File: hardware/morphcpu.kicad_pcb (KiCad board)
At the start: 2 copper layers, 70 x 70 mm, 84 parts, among them J1 TYPE-C-31-M-12, SW1 TS-1187A-B-A-B, U1 ICE40UP5K-SG48I, U2 FT231XS-R, U3 W25Q32JVSSIQ, U4 ME6211C33M5G-N, U5 ME6211C12M5G-N, U6 USBLC6-2SC6, X1 1532H4-16000JWPDTSNL

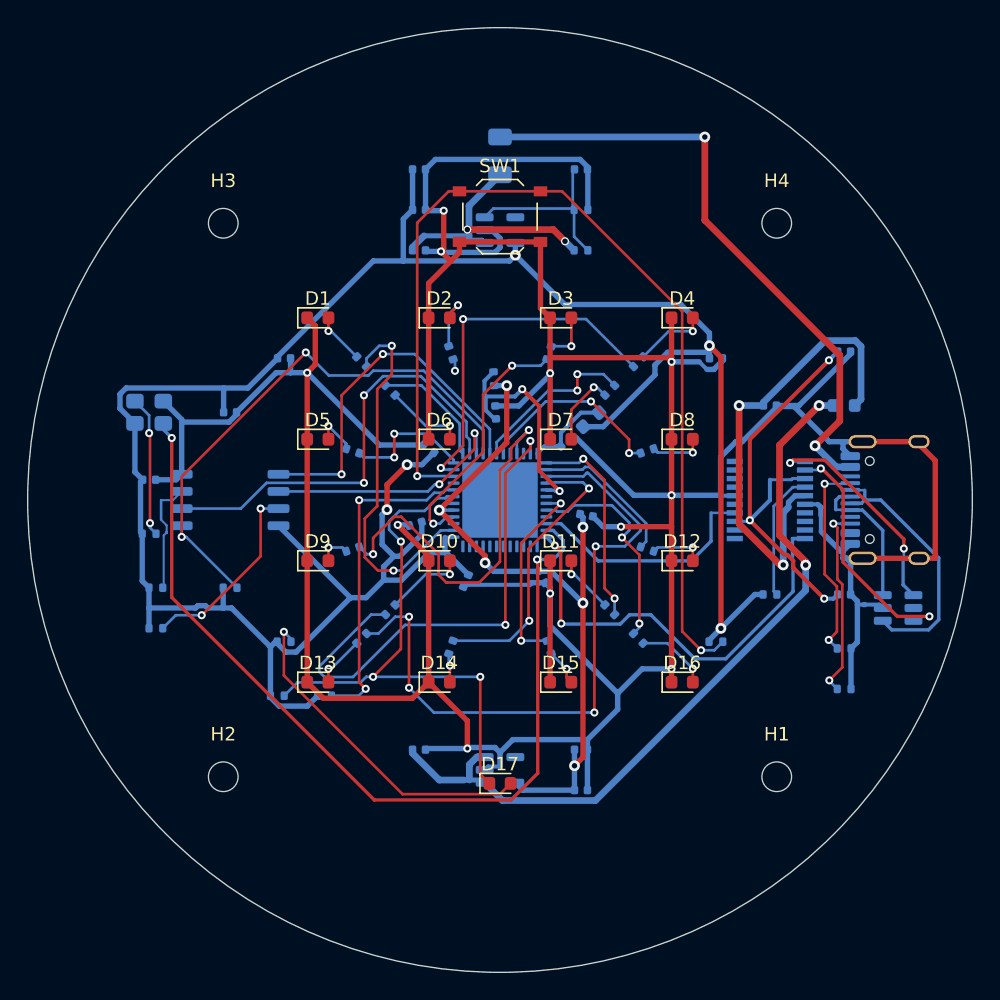
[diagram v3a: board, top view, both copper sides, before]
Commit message: autoroute revert
board back to 0 tracks 0 zones. freerouting didnt come back clean and the front
face was a mess, so its out. kept the DSN, the SES and the renders, wrote up
what happened in ROUTING.md.

DRC after: 1 cosmetic silk, 167 unconnected. ERC 0/0. generators run, tests pass.

also went over every .md .py .sh .v .pcf .scad. contractions, unicode arrows to
ascii, comment divider scaffolding out. no number or part number or path
changed, tables left alone, $display and RESULT:/PASS: strings untouched cause
run_sims.sh reads them.
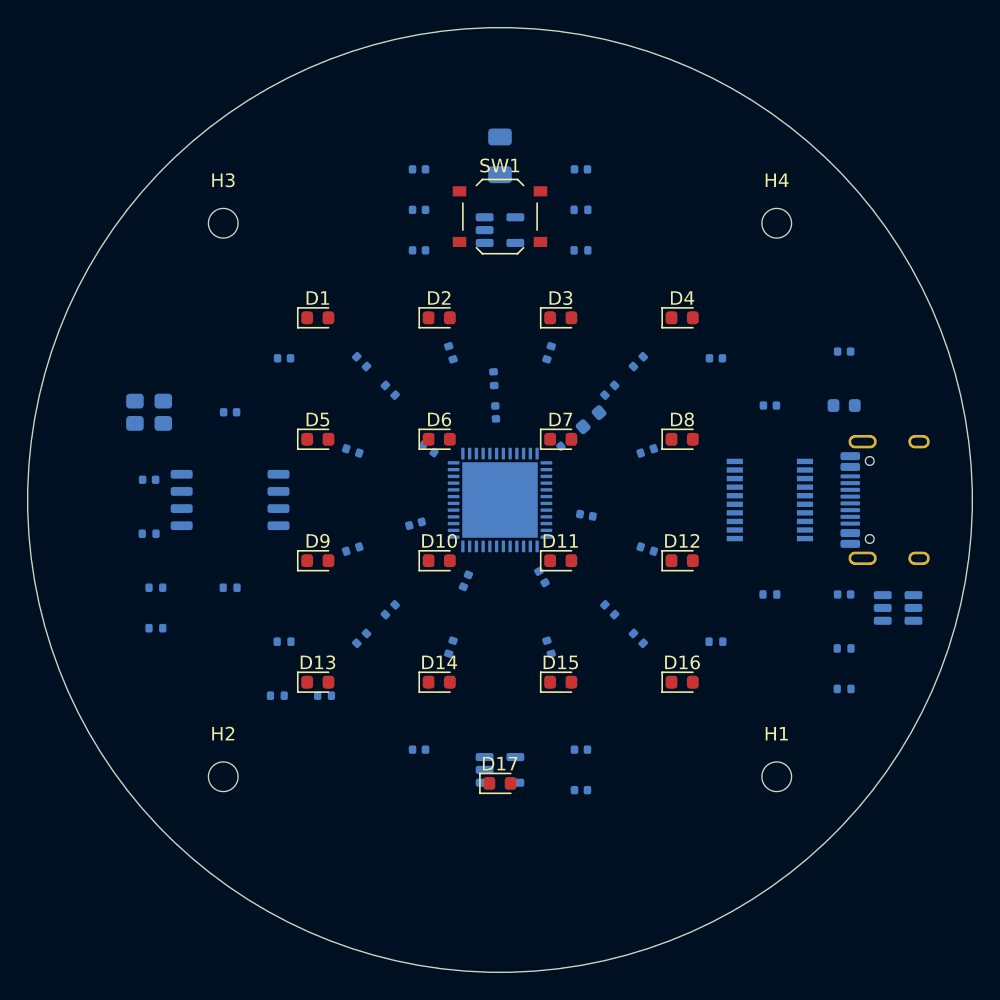
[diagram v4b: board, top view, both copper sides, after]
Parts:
- turned C2 to -61.4286 degrees
- turned C4 to -164.286 degrees
- turned C21 to 41.4286 degrees
- turned R8 to 18.4349 degrees
- turned R14 to -108.435 degrees
- turned R12 to -18.4349 degrees
- turned R15 to -71.5651 degrees
- turned R2 to 108.435 degrees
- turned R5 to 161.565 degrees
- turned R3 to 71.5651 degrees
- turned R9 to -161.565 degrees
- turned C5 to 144.286 degrees
- turned C3 to -112.857 degrees
- turned C20 to 92.8571 degrees
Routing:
- net GND: track 339.1 -> 0.00 mm, vias 11 -> 0
- net +3V3: track 183.2 -> 0.00 mm, vias 5 -> 0
- net VBUS: track 77.1 -> 0.00 mm, vias 4 -> 0
- net RST_N: track 73.3 -> 0.00 mm, vias 2 -> 0
- net CLK: track 67.6 -> 0.00 mm, vias 2 -> 0
- net +1V2: track 53.7 -> 0.00 mm, vias 6 -> 0
- net LED12: track 48.7 -> 0.00 mm, vias 4 -> 0
- net VBUS_IN: track 46.2 -> 0.00 mm, vias 2 -> 0
- net CDONE: track 41.6 -> 0.00 mm, vias 3 -> 0
- net FLASH_CS: track 41.5 -> 0.00 mm, vias 2 -> 0
- net LED9: track 37.8 -> 0.00 mm, vias 2 -> 0
- net FT_VCC: track 35.5 -> 0.00 mm, vias 2 -> 0
- net UART_RX_I: track 33.5 -> 0.00 mm, vias 2 -> 0
- net FLASH_DO: track 32.8 -> 0.00 mm, vias 2 -> 0
- net FT_3V3: track 32.0 -> 0.00 mm, vias 3 -> 0
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
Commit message: 4 layers / board routes now
2 layers was the problem, not the router. the resistor ring sits at r 11-15 and
the decap ring at r 6-7, both inside the F.Cu keepout, so all 16 LED escapes
plus every supply converging on U1 had exactly one layer to share. seven
freerouting configs, a maze router, a rip-up loop and a pathfinder
implementation all bounced off that.

stackup is F.Cu / In1.Cu / In2.Cu / B.Cu, both inner layers signal. In1 was a
power plane first and freerouting wont route on a power layer, so it only used
In2 and came back at 13 unrouted. flipping In1 to signal got it to 11

  DRC   1 violation, the same cosmetic C20/R27 silk overlap thats been there
        since the resistor ring moved. zero clearance, zero hole, zero thermal
  unconnected  17 items

  F.Cu    39 segments
  In1.Cu  77
  In2.Cu 100
  B.Cu   366
  vias   130

front face is clean and it actually verifies now:

  keepout violations in DRC                            0
  F.Cu segments with copper in the no-track region     0

checked twice, once by DRC and once by walking 20 points along every F.Cu
segment against the escape windows. 39 F.Cu segments on the whole board and
none of them cross the display

min track width went 0.1524 -> 0.127. freerouting kept emitting 0.15 mm and 5
mil is JLC's economical tier for 2 layer anyway, so its free. that cleared 10
track_width errors

the 17 unconnected are 5 connections my router couldnt place, all U1 escapes,
U1-30 to C1-1, U1-30 to U1-5, U1-29 to C20-1, R13-1 to U1-27, R16-1 to U1-32,
plus a VBUS_IN via that needs a pad. hand route them, theyre short

LED2 got routed and then ripped back out, 139 segments of meander that pulled
12 clearance errors with it. one connection for twelve violations wasnt worth
keeping

what didnt work, so nobody repeats it. narrower traces made it worse, 15 -> 18.
300 passes and a different search strategy gave byte identical output to 100
passes. a centre disc in the keepout bought exactly one net. grafting a route
back 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
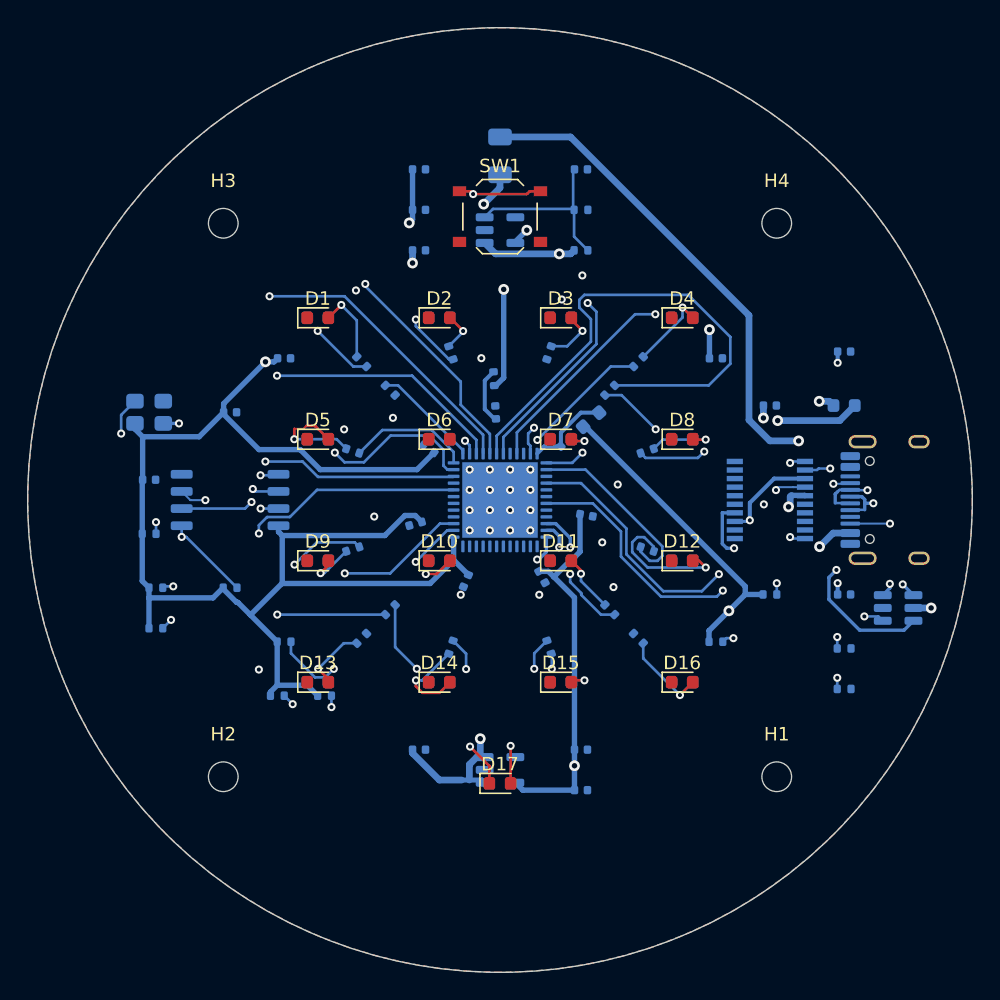
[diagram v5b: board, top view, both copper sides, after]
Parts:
- turned C2 to -61.429 degrees
- turned C4 to -164.286 degrees
- turned C21 to 41.429 degrees
- turned R8 to 18.435 degrees
- turned R14 to -108.435 degrees
- turned R12 to -18.435 degrees
- turned R15 to -71.565 degrees
- turned R2 to 108.435 degrees
- turned R5 to 161.565 degrees
- turned R3 to 71.565 degrees
- turned R9 to -161.565 degrees
- turned C5 to 144.286 degrees
- turned C3 to -112.857 degrees
- turned C20 to 92.857 degrees
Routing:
- net +3V3: track 0.00 -> 194.9 mm, vias 0 -> 5
- net VBUS: track 0.00 -> 119.3 mm, vias 0 -> 6
- net RST_N: track 0.00 -> 92.5 mm, vias 0 -> 3
- net +1V2: track 0.00 -> 72.8 mm, vias 0 -> 2
- net LED8: track 0.00 -> 68.1 mm, vias 0 -> 5
- net FLASH_CS: track 0.00 -> 49.2 mm, vias 0 -> 2
- net VBUS_IN: track 0.00 -> 47.2 mm, vias 0 -> 2
- net LED0: track 0.00 -> 47.0 mm, vias 0 -> 2
- net LED13: track 0.00 -> 41.9 mm, vias 0 -> 2
- net LED9: track 0.00 -> 40.1 mm, vias 0 -> 3
- net LED6: track 0.00 -> 38.5 mm
- net FLASH_DI: track 0.00 -> 36.5 mm, vias 0 -> 2
- net LED3: track 0.00 -> 36.4 mm, vias 0 -> 2
- net LED14: track 0.00 -> 36.1 mm, vias 0 -> 2
- net CLK: track 0.00 -> 35.9 mm, vias 0 -> 2
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- added copper zone on B.Cu, net GND
- added copper zone on F.Cu, net GND
- added copper zone on In1.Cu, net GND
- added copper zone on In2.Cu, net GND
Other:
- copper layers 2 -> 4

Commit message: route 7 of the 17 outstanding connections, DRC to 0 violations
Adds 84 segments and 11 vias for seven connections: the GND pour fragments at
C4.2, C12.2 and C7.2 (C7 also resolves U3.4, same island), plus VCCPLL_F,
VBUS_IN, LED2 and LED15. Nothing already on the board was moved.

Every placed segment and via was exact-clearance checked against all foreign
copper before being committed, and the no-track rule area is honoured as
outline-minus-holes. VBUS_IN came out at 0.30 mm against its 0.50 mm PWR_5V
class - still 1.00 A by IPC-2221 against a 500 mA polyfuse, but it drops the
intended ~2.9x margin to ~2x, so it is worth a look by hand.

Also moves C20's reference field 1.3 mm in X, clearing the silk overlap with
R27 that was the last standing violation.

DRC, with the .kicad_pro alongside: 1 violation / 17 unconnected -> 0 / 10.

Six of the ten that remain cannot be routed by adding copper at all - U1.22
has 51 reachable grid cells and no via fits - and need the U1 fanout ripped up
first. ROUTING.md records the per-connection reachability analysis and why
both a grid maze router and a second Freerouting pass fell short.
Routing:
- net LED2: track 0.00 -> 22.3 mm, vias 0 -> 3
- net LED15: track 0.00 -> 12.2 mm, vias 0 -> 2
- net VCCPLL_F: track 4.16 -> 14.8 mm, vias 0 -> 2
- net VBUS_IN: track 47.2 -> 53.1 mm, vias 2 -> 3
- net GND: track 0.00 -> 2.41 mm, vias 24 -> 27

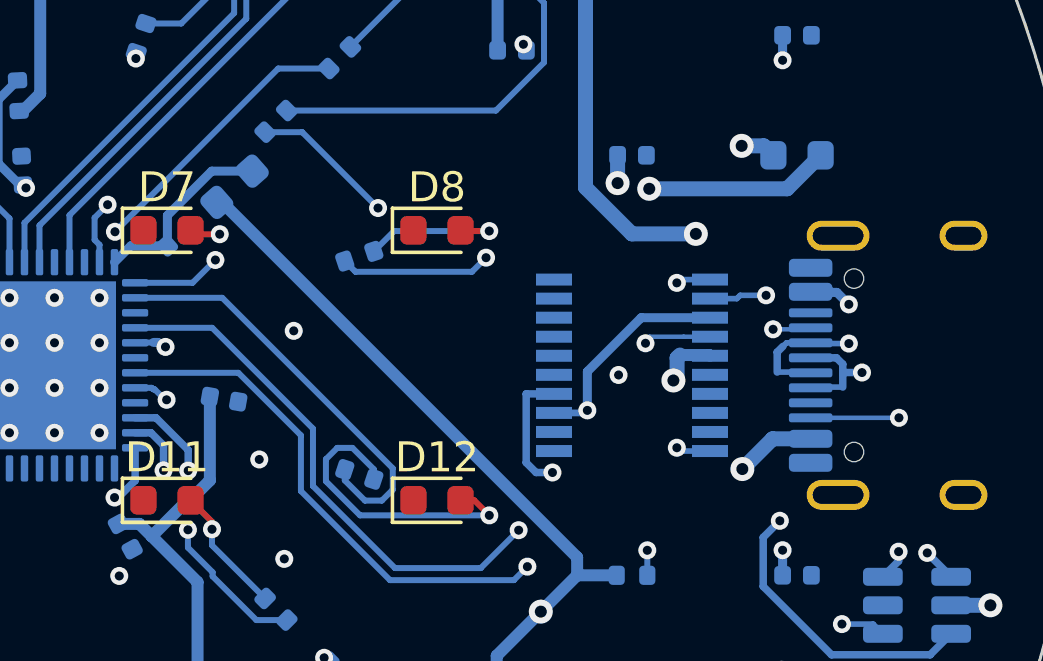
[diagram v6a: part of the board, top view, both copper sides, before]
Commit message: route 2 of the 10 outstanding: GND at C21.2 and U2.16
Both pads sit in a small isolated B.Cu pour island with the main In1/In2/F
planes running straight underneath, so what they needed was one stitching via
each, not a route. Neither had a legal through-via site: a via must clear all
four layers, and the inner layers were covered.

C21.2 had four free sites all along - the earlier search missed them because
the 0.05 mm raster marks a cell blocked when its centre falls inside the
inflated obstacle, which is up to half a cell pessimistic. The router now
rasterises half a cell optimistic and lets exact pcbnew clearance be the
authority, vetoing rejected cells and re-routing.

U2.16 was walled on In2 by the VBUS_IN leg running down the middle of its
pocket, so VBUS_IN was ripped and rebuilt around the new via. That also lifts
VBUS_IN off the 0.30 mm it had necked to; it is 0.40 mm now against its
0.50 mm PWR_5V class.

USB_DP/DM and CC1/CC2 verified byte-identical.

0 violations, 10 unconnected -> 0 violations, 8 unconnected.
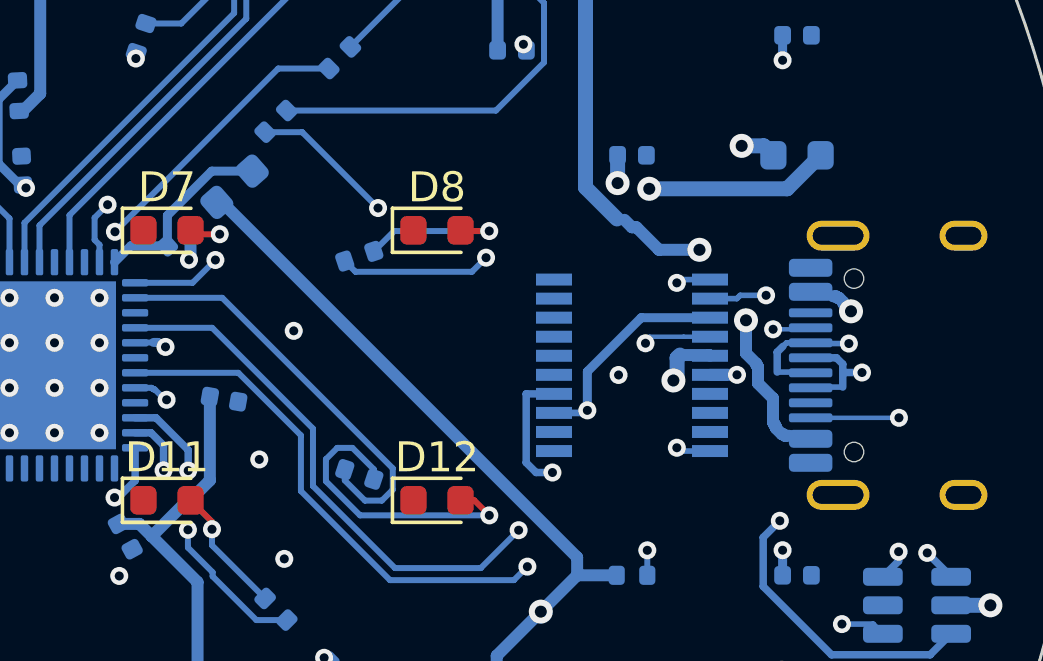
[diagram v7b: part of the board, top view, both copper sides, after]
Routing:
- net VBUS_IN: track 53.1 -> 49.6 mm
- net GND: track 2.41 -> 4.70 mm, vias 27 -> 29

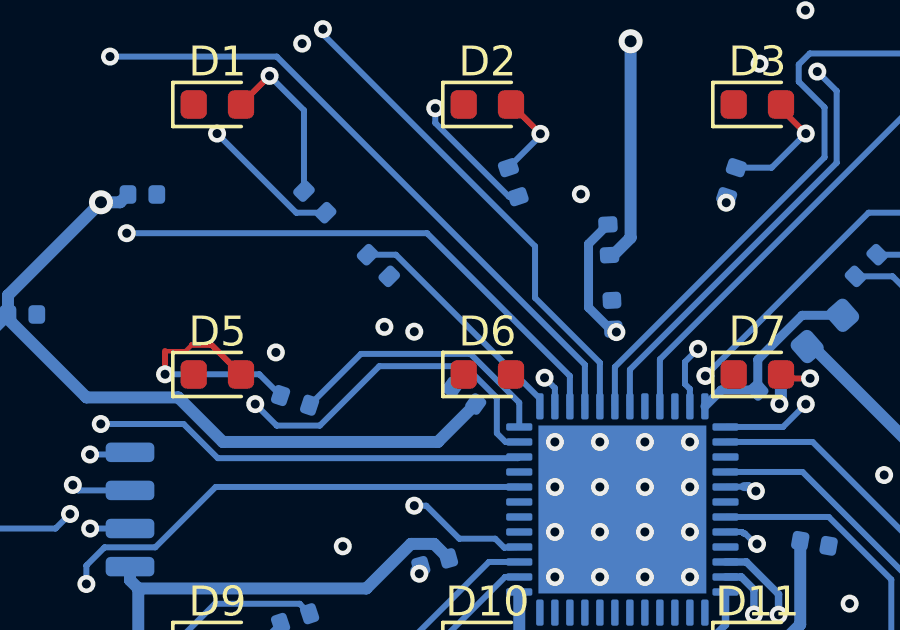
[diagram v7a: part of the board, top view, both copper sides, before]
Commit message: route LED5_A, the last one that did not need the U1 fanout moved
Falls out standalone now that the router rasterises half a cell optimistic and
lets exact pcbnew clearance arbitrate. 8 segments and 3 vias, R6.2 on B.Cu up
to D6.2 on F.Cu.

0 violations, 8 unconnected -> 0 violations, 7 unconnected.
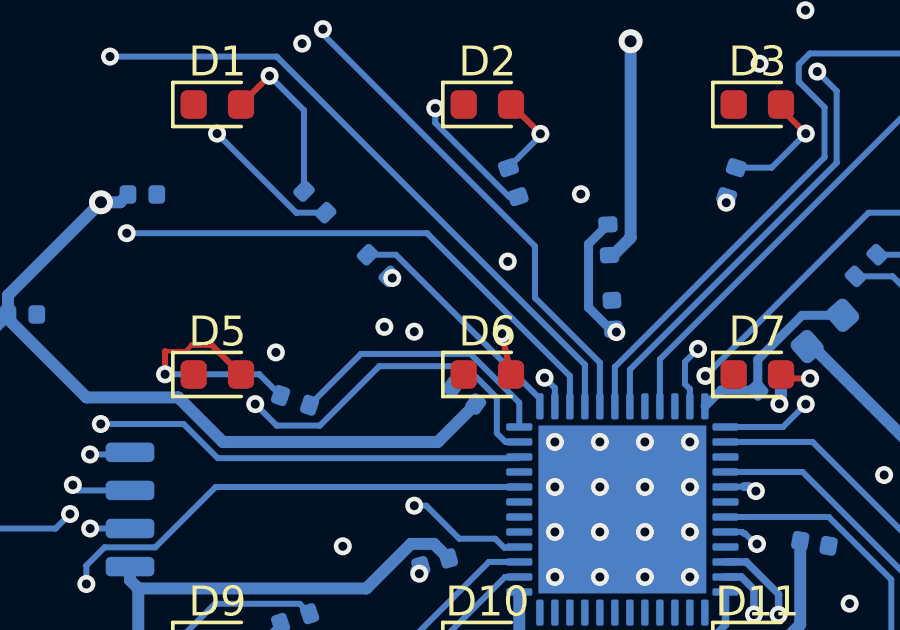
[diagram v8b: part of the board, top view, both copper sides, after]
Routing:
- net LED5_A: track 0.00 -> 8.06 mm, vias 0 -> 3
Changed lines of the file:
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@@
+	)
+	(segment
+		(start 145.978924 94.135174)
+		(end 146.2875 95.5)
+		(width 0.2)
+		(layer "F.Cu")
+		(net "LED5_A")
+	)
+	(via
+		(at 146.178924 91.735174)
+		(size 0.6)
+		(drill 0.3)
+		(layers "F.Cu" "B.Cu")
+		(net "LED5_A")
+	)
+	(via
+		(at 145.978924 94.135174)
+		(size 0.6)
+		(drill 0.3)
+		(layers "F.Cu" "B.Cu")
+		(net "LED5_A")
+	)
+	(via
+		(at 142.328924 92.285174)
+		(size 0.6)
+		(drill 0.3)
+		(layers "F.Cu" "B.Cu")
+		(net "LED5_A")
+	)
+	(segment
+		(start 142.228924 92.228924)
+		(end 142.878924 92.285174)
+		(width 0.2)
+		(layer "In1.Cu")
+		(net "LED5_A")
+	)
+	(segment
+		(start 144.878924 91.785174)
+		(end 144.928924 91.735174)
+		(width 0.2)
+		(layer "In1.Cu")
+		(net "LED5_A")
+	)
+	(segment
+		(start 143.378924 91.785174)
+		(end 144.878924 91.785174)
+		(width 0.2)
+		(layer "In1.Cu")
+		(net "LED5_A")
+	)
+	(segment
+		(start 142.878924 92.285174)
+		(end 143.378924 91.785174)
+		(width 0.2)
+		(layer "In1.Cu")
+		(net "LED5_A")
+	)
+	(segment
+		(start 144.928924 91.735174)
+		(end 146.178924 91.735174)
+		(width 0.2)
+		(layer "In1.Cu")
+		(net "LED5_A")
+	)
+	(segment
+		(start 146.178924 93.935174)
+		(end 145.978924 94.135174)
+		(width 0.2)
+		(layer "In2.Cu")
+		(net "LED5_A")
+	)
+	(segment
+		(start 146.178924 91.735174)
+		(end 146.178924 93.935174)
+		(width 0.2)
+		(layer "In2.Cu")
+		(net "LED5_A")
 	)
 	(segment
